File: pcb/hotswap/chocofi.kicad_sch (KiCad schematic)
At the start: 53 parts, among them J1 MJ-4PP-9, J2 Conn_01x04, J3 Conn_01x02_Female, SW1 SW_SPDT, SW10 SW_PUSH, SW11 SW_PUSH, SW12 SW_PUSH, SW14 SW_PUSH, SW15 SW_PUSH, SW16 SW_PUSH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

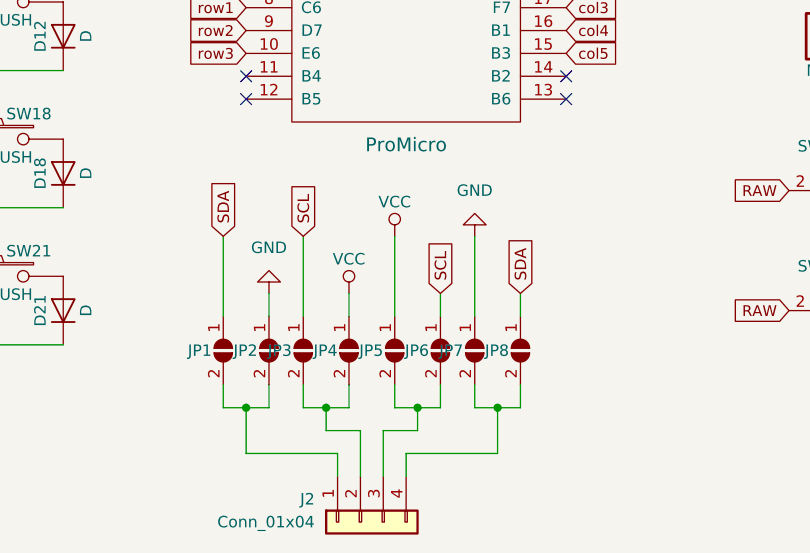
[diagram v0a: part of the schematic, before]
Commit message: Add niceview support, move power switch
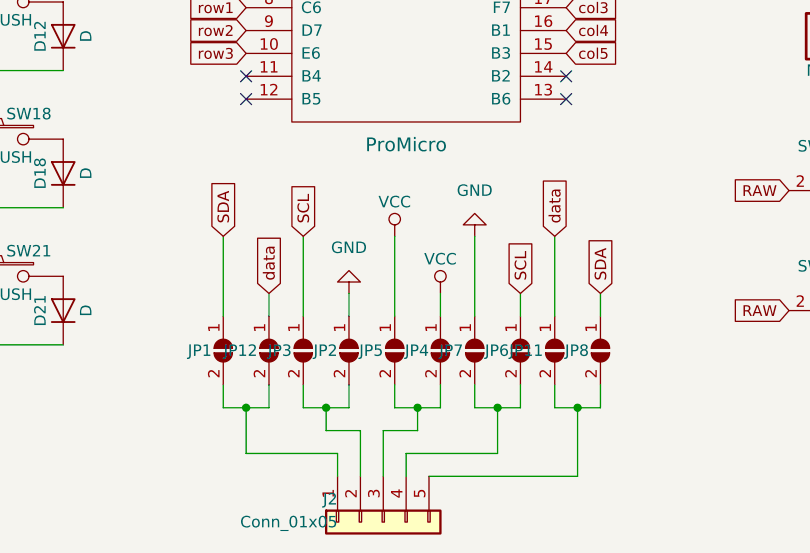
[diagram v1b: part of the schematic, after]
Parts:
- added JP11, JP12: CS, kbd:Jumper, symbol Jumper:SolderJumper_2_Open
- J2: value Conn_01x04 -> Conn_01x05; footprint kbd:OLED -> nice_view:nice_view_1side; symbol Connector_Generic:Conn_01x04 -> Connector_Generic:Conn_01x05
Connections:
- net data: now also JP11.1 (A), JP12.1 (A)
- net at J2.2 (Pin_2), JP3.2 (B): now also JP2.2 (B); no longer JP4.2 (B)
- net at J2.1 (Pin_1), JP1.2 (B): now also JP12.2 (B); no longer JP2.2 (B)
- net at J2.4 (Pin_4), JP7.2 (B): now also JP6.2 (B); no longer JP8.2 (B)
- net at J2.3 (Pin_3), JP5.2 (B): now also JP4.2 (B); no longer JP6.2 (B)
- new net: J2.5 (Pin_5), JP11.2 (B), JP8.2 (B)
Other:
- moved on the sheet: JP2, JP4, JP6, JP8
